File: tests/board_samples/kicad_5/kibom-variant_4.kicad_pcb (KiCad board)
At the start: 2 copper layers, 12.7 x 10.2 mm, 5 parts

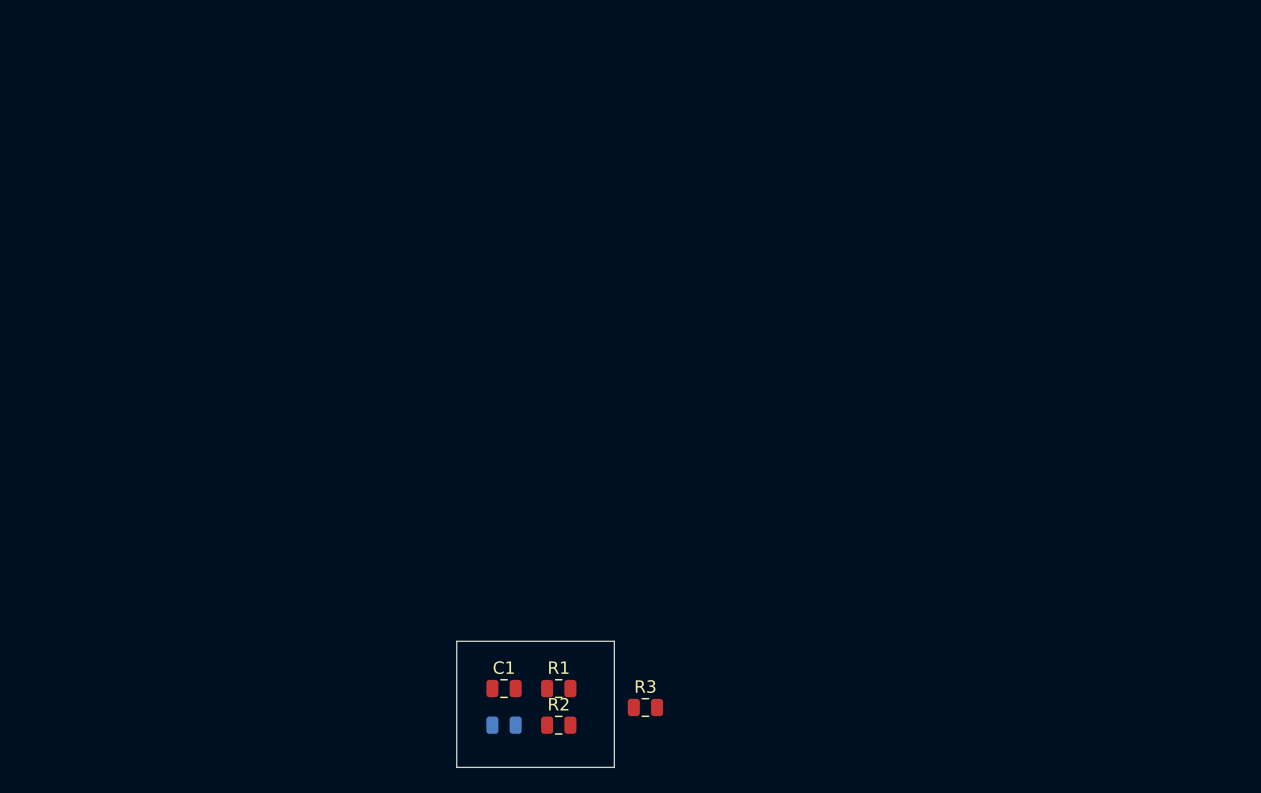
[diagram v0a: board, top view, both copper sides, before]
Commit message: Test case for 3D Model variants, and for empty dnp, kicost variants for non existing fields
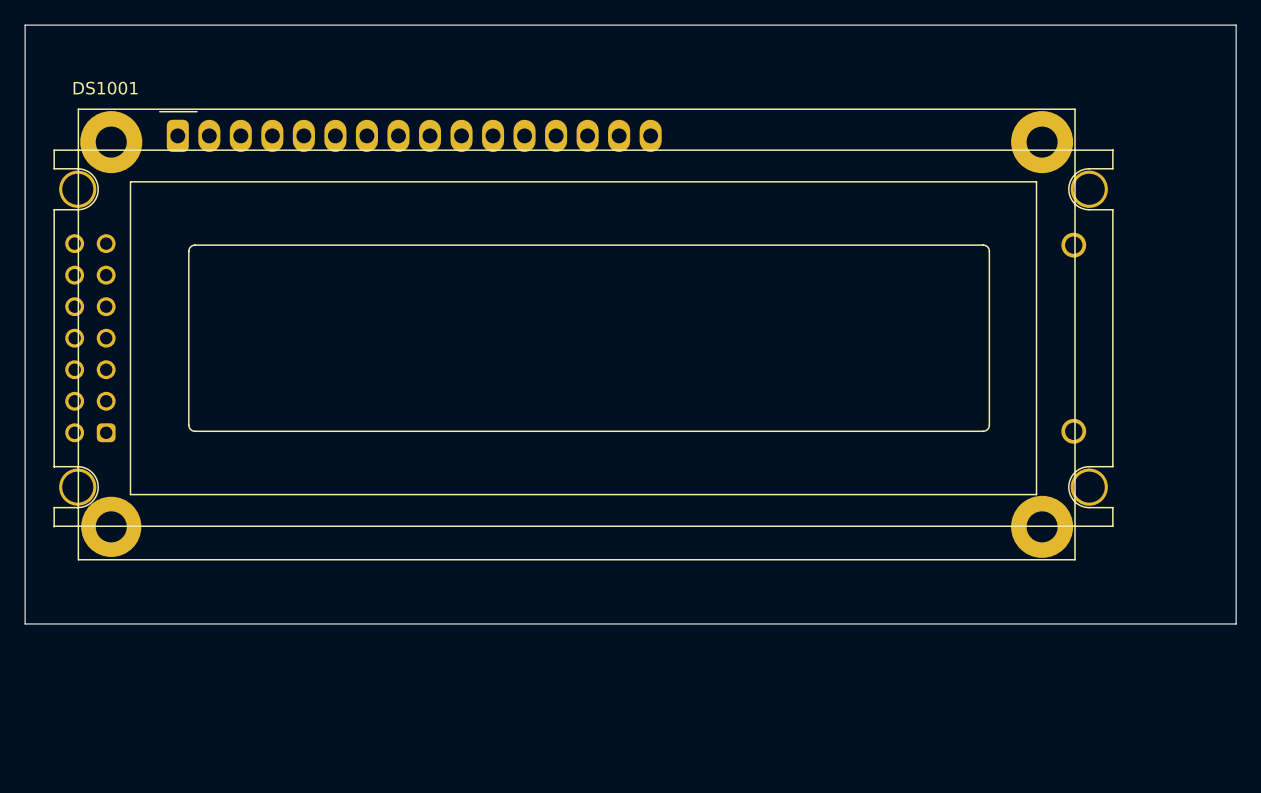
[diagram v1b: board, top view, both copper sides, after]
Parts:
- removed C1: 1nF, Capacitor_SMD:C_0805_2012Metric
- removed C2: 1000 pF, Capacitor_SMD:C_0805_2012Metric
- removed R1, R3: 1k, Resistor_SMD:R_0805_2012Metric
- removed R2: 1000, Resistor_SMD:R_0805_2012Metric
- added DS1001: **Val, kibom-variant_4:LCD_16x02_Dual, F.Cu at (110.9, 43.1)
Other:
- board size 12.7 x 10.2 mm -> 97.6 x 48.2 mm
- board text removed: "Bogus component. Not in schematic."

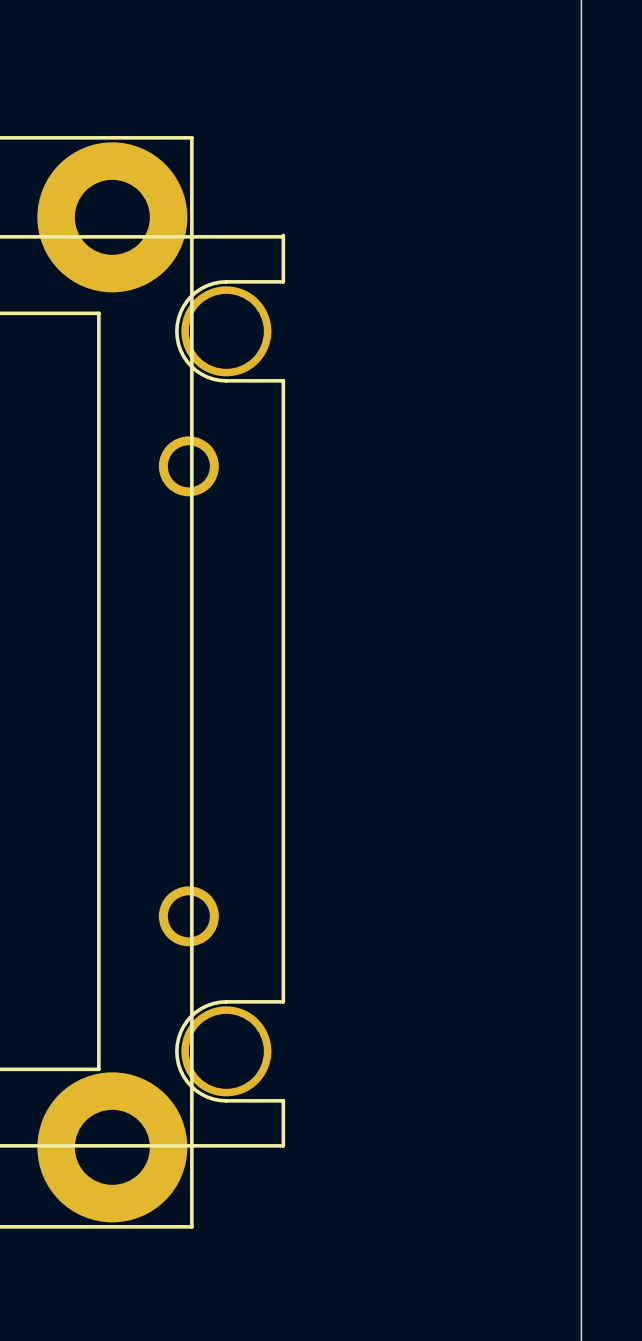
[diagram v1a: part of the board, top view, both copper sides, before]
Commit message: Update schematic & PCB to use more recent 3D models
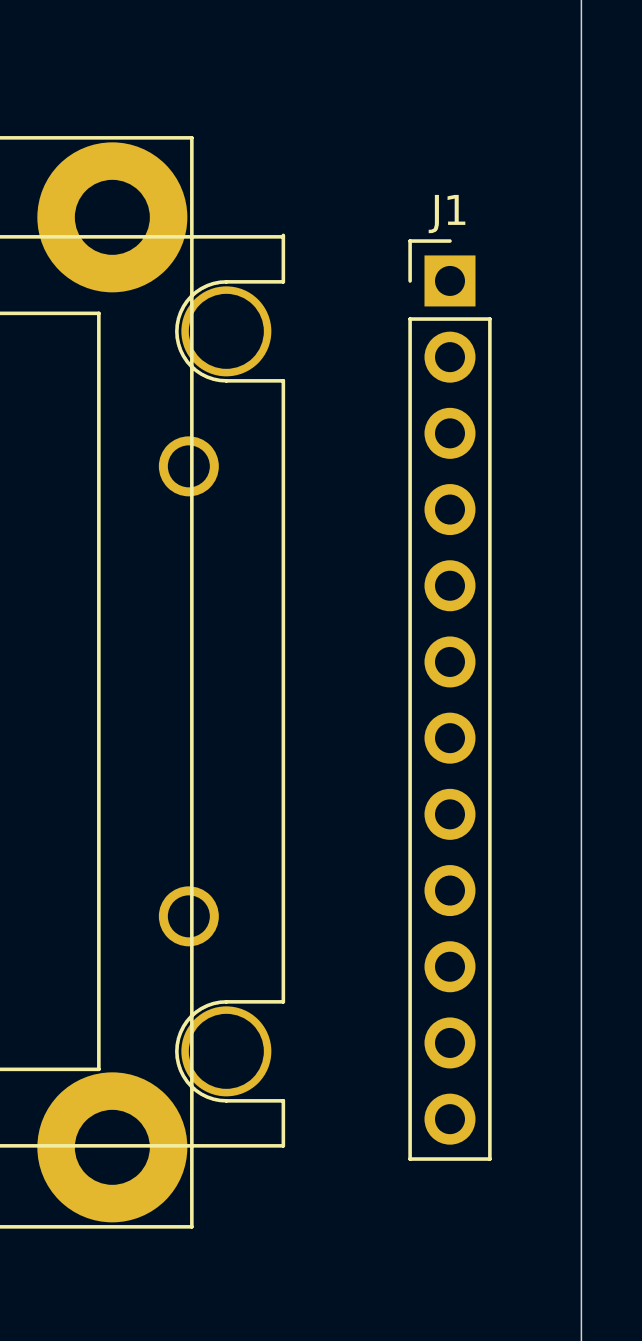
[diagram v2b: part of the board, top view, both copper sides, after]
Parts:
- added J1: Conn_01x12_Female, Connector_PinHeader_2.54mm:PinHeader_1x12_P2.54mm_Vertical, F.Cu at (191.8, 45.7)
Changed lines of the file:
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@@
     (tracks 0)
     (zones 0)
-    (modules 1)
-    (nets 17)
+    (modules 2)
+    (nets 29)
   )
   (page A4)
@@
   (net 15 "Net-(DS1001-Pad2)")
   (net 16 "Net-(DS1001-Pad1)")
+  (net 17 "Net-(J1-Pad12)")
+  (net 18 "Net-(J1-Pad11)")
+  (net 19 "Net-(J1-Pad10)")
+  (net 20 "Net-(J1-Pad9)")
+  (net 21 "Net-(J1-Pad8)")
+  (net 22 "Net-(J1-Pad7)")
+  (net 23 "Net-(J1-Pad6)")
+  (net 24 "Net-(J1-Pad5)")
+  (net 25 "Net-(J1-Pad4)")
+  (net 26 "Net-(J1-Pad3)")
+  (net 27 "Net-(J1-Pad2)")
+  (net 28 "Net-(J1-Pad1)")
   (net_class Default "This is the default net class."
     (clearance 0.2)
@@
     (add_net "Net-(DS1001-Pad8)")
     (add_net "Net-(DS1001-Pad9)")
+    (add_net "Net-(J1-Pad1)")
+    (add_net "Net-(J1-Pad10)")
+    (add_net "Net-(J1-Pad11)")
+    (add_net "Net-(J1-Pad12)")
+    (add_net "Net-(J1-Pad2)")
+    (add_net "Net-(J1-Pad3)")
+    (add_net "Net-(J1-Pad4)")
+    (add_net "Net-(J1-Pad5)")
+    (add_net "Net-(J1-Pad6)")
+    (add_net "Net-(J1-Pad7)")
+    (add_net "Net-(J1-Pad8)")
+    (add_net "Net-(J1-Pad9)")
   )
   (module kibom-variant_4:LCD_16x02_Dual (layer F.Cu)
@@
       (rotate (xyz 0 0 0))
     )
-    (model ${KISYS3DMOD}/Pin_Headers.3dshapes/Pin_Header_Straight_2x07_Pitch2.54mm.wrl
-      (offset (xyz -5.925 -8.699999999999999 4.4))
-      (scale (xyz 1 1 1))
-      (rotate (xyz 180 0 180))
-    )
-    (model ${KISYS3DMOD}/Pin_Headers.3dshapes/Pin_Header_Straight_1x16_Pitch2.54mm.wrl
+    (model ${KISYS3DMOD}/Connector_PinHeader_2.54mm.3dshapes/PinHeader_2x07_P2.54mm_Vertical.wrl
+      (offset (xyz -8.465 -8.699999999999999 0))
+      (scale (xyz 1 1 1))
+      (rotate (xyz 0 0 0))
+    )
+    (model ${KISYS3DMOD}/Connector_PinHeader_2.54mm.3dshapes/PinHeader_1x16_P2.54mm_Vertical.wrl
       (offset (xyz 0 0 4.2))
       (scale (xyz 1 1 1))
       (rotate (xyz 180 0 90))
     )
-    (model ${KISYS3DMOD}/Pin_Headers.3dshapes/Pin_Header_Straight_1x01_Pitch2.54mm.wrl
+    (model ${KISYS3DMOD}/Connector_PinHeader_2.54mm.3dshapes/PinHeader_1x01_P2.54mm_Vertical.wrl
       (offset (xyz 72.05 -8.800000000000001 4.4))
       (scale (xyz 1 1 1))
       (rotate (xyz 180 0 0))
     )
-    (model ${KISYS3DMOD}/Pin_Headers.3dshapes/Pin_Header_Straight_1x01_Pitch2.54mm.wrl
+    (model ${KISYS3DMOD}/Connector_PinHeader_2.54mm.3dshapes/PinHeader_1x01_P2.54mm_Vertical.wrl
       (offset (xyz 72.05 -23.8 0))
       (scale (xyz 1 1 1))
@@
       (rotate (xyz 0 0 0))
     )
-    (model ${KISYS3DMOD}/Pin_Headers.3dshapes/Pin_Header_Straight_2x07_Pitch2.54mm%leftvariant%.wrl
-      (offset (xyz -5.925 -8.699999999999999 4.4))
-      (scale (xyz 1 1 1))
-      (rotate (xyz 180 0 180))
-    )
-    (model ${KISYS3DMOD}/Pin_Headers.3dshapes/Pin_Header_Straight_1x16_Pitch2.54mm%topvariant%.wrl
+    (model ${KISYS3DMOD}/Connector_PinHeader_2.54mm.3dshapes/PinHeader_2x07_P2.54mm_Vertical%leftvariant%.wrl
+      (offset (xyz -8.465 -8.699999999999999 0))
+      (scale (xyz 1 1 1))
+      (rotate (xyz 0 0 0))
+    )
+    (model ${KISYS3DMOD}/Connector_PinHeader_2.54mm.3dshapes/PinHeader_1x16_P2.54mm_Vertical%topvariant%.wrl
       (offset (xyz 0 0 4.2))
       (scale (xyz 1 1 1))
       (rotate (xyz 180 0 90))
     )
-    (model ${KISYS3DMOD}/Pin_Headers.3dshapes/Pin_Header_Straight_1x01_Pitch2.54mm%leftvariant%.wrl
+    (model ${KISYS3DMOD}/Connector_PinHeader_2.54mm.3dshapes/PinHeader_1x01_P2.54mm_Vertical%leftvariant%.wrl
       (offset (xyz 72.05 -8.800000000000001 4.4))
       (scale (xyz 1 1 1))
       (rotate (xyz 180 0 0))
     )
-    (model ${KISYS3DMOD}/Pin_Headers.3dshapes/Pin_Header_Straight_1x01_Pitch2.54mm%leftvariant%.wrl
+    (model ${KISYS3DMOD}/Connector_PinHeader_2.54mm.3dshapes/PinHeader_1x01_P2.54mm_Vertical%leftvariant%.wrl
       (offset (xyz 72.05 -23.8 0))
       (scale (xyz 1 1 1))
@@
       (scale (xyz 1 1 1))
       (rotate (xyz 0 0 0))
+    )
+  )
+  (module Connector_PinHeader_2.54mm:PinHeader_1x12_P2.54mm_Vertical (layer F.Cu)
+    (at 191.77 45.72)
+    (descr "Through hole straight pin header, 1x12, 2.54mm pitch, single row")
+    (tags "Through hole pin header THT 1x12 2.54mm single row")
+    (fp_text reference J1 (at 0 -2.33) (layer F.SilkS)
+      (effects (font (size 1 1) (thickness 0.15)))
+    )
+    (fp_text value Conn_01x12_Female (at 0 30.27) (layer F.Fab)
+      (effects (font (size 1 1) (thickness 0.15)))
+    )
+    (fp_line (start 1.8 -1.8) (end -1.8 -1.8) (layer F.CrtYd) (width 0.05))
+    (fp_line (start 1.8 29.75) (end 1.8 -1.8) (layer F.CrtYd) (width 0.05))
+    (fp_line (start -1.8 29.75) (end 1.8 29.75) (layer F.CrtYd) (width 0.05))
+    (fp_line (start -1.8 -1.8) (end -1.8 29.75) (layer F.CrtYd) (width 0.05))
+    (fp_line (start -1.33 -1.33) (end 0 -1.33) (layer F.SilkS) (width 0.12))
+    (fp_line (start -1.33 0) (end -1.33 -1.33) (layer F.SilkS) (width 0.12))
+    (fp_line (start -1.33 1.27) (end 1.33 1.27) (layer F.SilkS) (width 0.12))
+    (fp_line (start 1.33 1.27) (end 1.33 29.27) (layer F.SilkS) (width 0.12))
+    (fp_line (start -1.33 1.27) (end -1.33 29.27) (layer F.SilkS) (width 0.12))
+    (fp_line (start -1.33 29.27) (end 1.33 29.27) (layer F.SilkS) (width 0.12))
+    (fp_line (start -1.27 -0.635) (end -0.635 -1.27) (layer F.Fab) (width 0.1))
+    (fp_line (start -1.27 29.21) (end -1.27 -0.635) (layer F.Fab) (width 0.1))
+    (fp_line (start 1.27 29.21) (end -1.27 29.21) (layer F.Fab) (width 0.1))
+    (fp_line (start 1.27 -1.27) (end 1.27 29.21) (layer F.Fab) (width 0.1))
+    (fp_line (start -0.635 -1.27) (end 1.27 -1.27) (layer F.Fab) (width 0.1))
+    (fp_text user %R (at 0 13.97 90) (layer F.Fab)
+      (effects (font (size 1 1) (thickness 0.15)))
+    )
+    (pad 12 thru_hole oval (at 0 27.94) (size 1.7 1.7) (drill 1) (layers *.Cu *.Mask)
+      (net 17 "Net-(J1-Pad12)"))
+    (pad 11 thru_hole oval (at 0 25.4) (size 1.7 1.7) (drill 1) (layers *.Cu *.Mask)
+      (net 18 "Net-(J1-Pad11)"))
+    (pad 10 thru_hole oval (at 0 22.86) (size 1.7 1.7) (drill 1) (layers *.Cu *.Mask)
+      (net 19 "Net-(J1-Pad10)"))
+    (pad 9 thru_hole oval (at 0 20.32) (size 1.7 1.7) (drill 1) (layers *.Cu *.Mask)
+      (net 20 "Net-(J1-Pad9)"))
+    (pad 8 thru_hole oval (at 0 17.78) (size 1.7 1.7) (drill 1) (layers *.Cu *.Mask)
+      (net 21 "Net-(J1-Pad8)"))
+    (pad 7 thru_hole oval (at 0 15.24) (size 1.7 1.7) (drill 1) (layers *.Cu *.Mask)
+      (net 22 "Net-(J1-Pad7)"))
+    (pad 6 thru_hole oval (at 0 12.7) (size 1.7 1.7) (drill 1) (layers *.Cu *.Mask)
+      (net 23 "Net-(J1-Pad6)"))
+    (pad 5 thru_hole oval (at 0 10.16) (size 1.7 1.7) (drill 1) (layers *.Cu *.Mask)
+      (net 24 "Net-(J1-Pad5)"))
+    (pad 4 thru_hole oval (at 0 7.62) (size 1.7 1.7) (drill 1) (layers *.Cu *.Mask)
+      (net 25 "Net-(J1-Pad4)"))
+    (pad 3 thru_hole oval (at 0 5.08) (size 1.7 1.7) (drill 1) (layers *.Cu *.Mask)
+      (net 26 "Net-(J1-Pad3)"))
+    (pad 2 thru_hole oval (at 0 2.54) (size 1.7 1.7) (drill 1) (layers *.Cu *.Mask)
+      (net 27 "Net-(J1-Pad2)"))
+    (pad 1 thru_hole rect (at 0 0) (size 1.7 1.7) (drill 1) (layers *.Cu *.Mask)
+      (net 28 "Net-(J1-Pad1)"))
+    (model ${KISYS3DMOD}/Connector_PinHeader_2.54mm.3dshapes/PinHeader_1x12_P2.54mm_Vertical.wrl
+      (at (xyz 0 0 0))
+      (scale (xyz 1 1 1))
+      (rotate (xyz 0 0 0))
